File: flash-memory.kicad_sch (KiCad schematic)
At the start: 4 parts, among them U3 W25Q64JVZEIQ

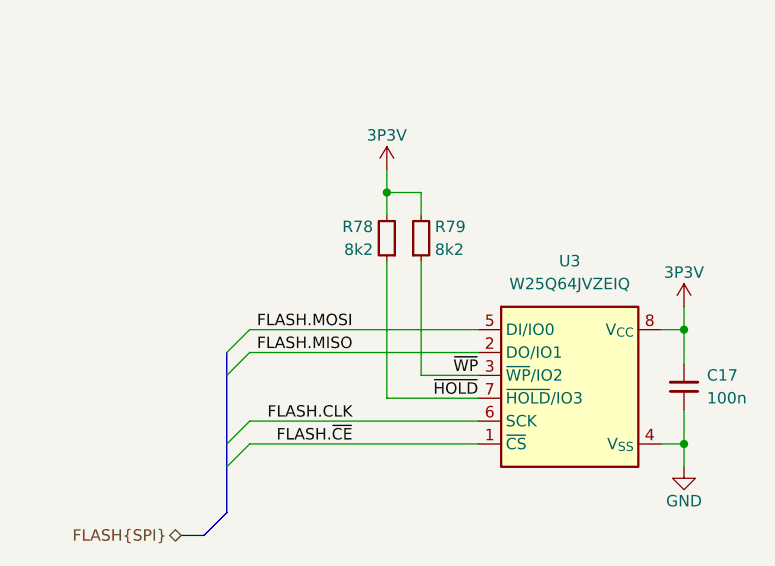
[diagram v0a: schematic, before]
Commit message: [#80813] Change RJ45 connectors, reannotate schematics
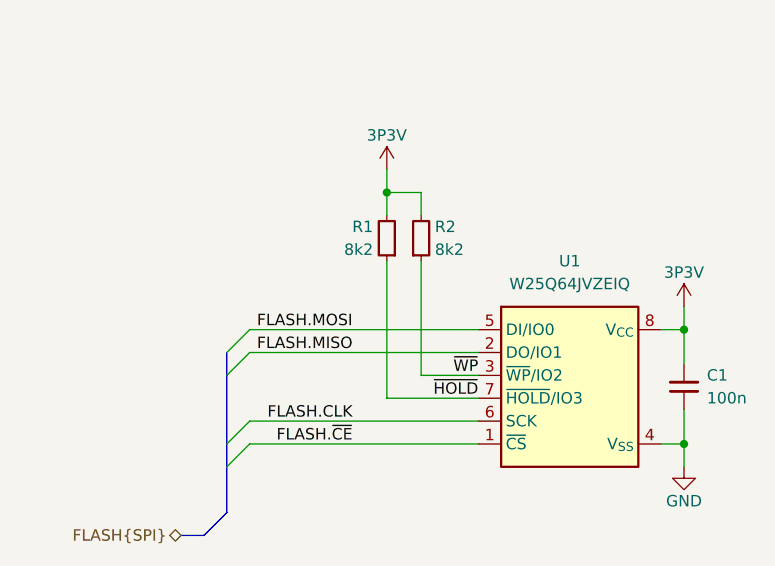
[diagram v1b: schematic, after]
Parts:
- renumbered C17 to C1, R78 to R1, R79 to R2, U3 to U1
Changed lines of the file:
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@@
 		(on_board yes)
 		(dnp no)
-		(property "Reference" "R78"
+		(property "Reference" "R1"
 			(at 191.516 132.08 90)
 			(effects
@@
 			(project ""
 				(path "/04bda987-e5eb-48b4-9e90-d8211dc11b39/cf61e8ef-a7e0-463f-9b69-1bf3871ad792"
-					(reference "R78")
+					(reference "R1")
 					(unit 1)
 				)
@@
 		(dnp no)
 		(fields_autoplaced yes)
-		(property "Reference" "U3"
+		(property "Reference" "U1"
 			(at 213.36 135.89 0)
 			(effects
@@
 			(project ""
 				(path "/04bda987-e5eb-48b4-9e90-d8211dc11b39/cf61e8ef-a7e0-463f-9b69-1bf3871ad792"
-					(reference "U3")
+					(reference "U1")
 					(unit 1)
 				)
@@
 		(on_board yes)
 		(dnp no)
-		(property "Reference" "#PWR076"
+		(property "Reference" "#PWR02"
 			(at 226.06 144.78 0)
 			(effects
@@
 			(project "10-gbe-expansion"
 				(path "/04bda987-e5eb-48b4-9e90-d8211dc11b39/cf61e8ef-a7e0-463f-9b69-1bf3871ad792"
-					(reference "#PWR076")
+					(reference "#PWR02")
 					(unit 1)
 				)
@@
 		(on_board yes)
 		(dnp no)
-		(property "Reference" "#PWR077"
+		(property "Reference" "#PWR01"
 			(at 193.04 129.54 0)
 			(effects
@@
 			(project "10-gbe-expansion"
 				(path "/04bda987-e5eb-48b4-9e90-d8211dc11b39/cf61e8ef-a7e0-463f-9b69-1bf3871ad792"
-					(reference "#PWR077")
+					(reference "#PWR01")
 					(unit 1)
 				)
@@
 		(dnp no)
 		(fields_autoplaced yes)
-		(property "Reference" "C17"
+		(property "Reference" "C1"
 			(at 228.6 148.5836 90)
 			(effects
@@
 			(project "10-gbe-expansion"
 				(path "/04bda987-e5eb-48b4-9e90-d8211dc11b39/cf61e8ef-a7e0-463f-9b69-1bf3871ad792"
-					(reference "C17")
+					(reference "C1")
 					(unit 1)
 				)
@@
 		(on_board yes)
 		(dnp no)
-		(property "Reference" "R79"
+		(property "Reference" "R2"
 			(at 198.374 132.08 90)
 			(effects
@@
 			(project "10-gbe-expansion"
 				(path "/04bda987-e5eb-48b4-9e90-d8211dc11b39/cf61e8ef-a7e0-463f-9b69-1bf3871ad792"
-					(reference "R79")
+					(reference "R2")
 					(unit 1)
 				)
@@
 		(on_board yes)
 		(dnp no)
-		(property "Reference" "#PWR075"
+		(property "Reference" "#PWR03"
 			(at 234.95 161.29 0)
 			(effects
@@
 			(project "10-gbe-expansion"
 				(path "/04bda987-e5eb-48b4-9e90-d8211dc11b39/cf61e8ef-a7e0-463f-9b69-1bf3871ad792"
-					(reference "#PWR075")
+					(reference "#PWR03")
 					(unit 1)
 				)

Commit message: [#80813] Change 3V3 and 1V88 power rails names
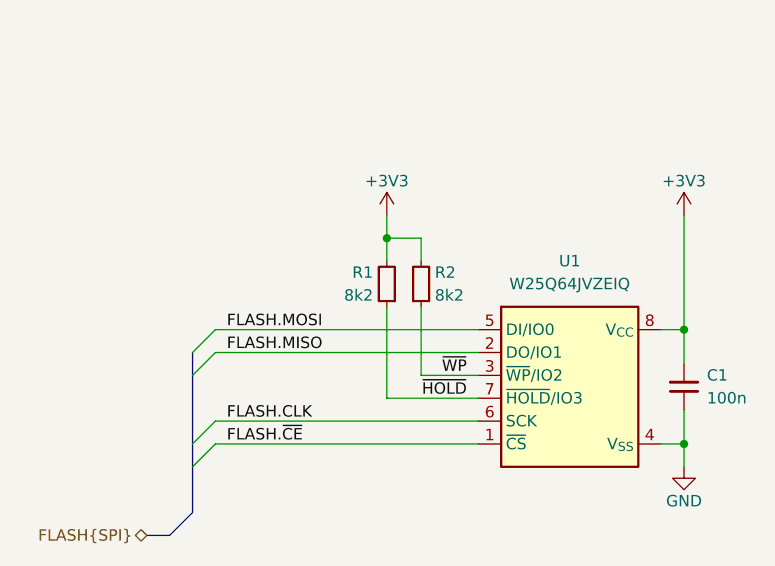
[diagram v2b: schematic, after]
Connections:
- net 3P3V renamed +3V3
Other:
- moved on the sheet: R1, R2

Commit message: [#80813] WIP: Adjust passives values, add missing load capacitors for the 50MHz resonator
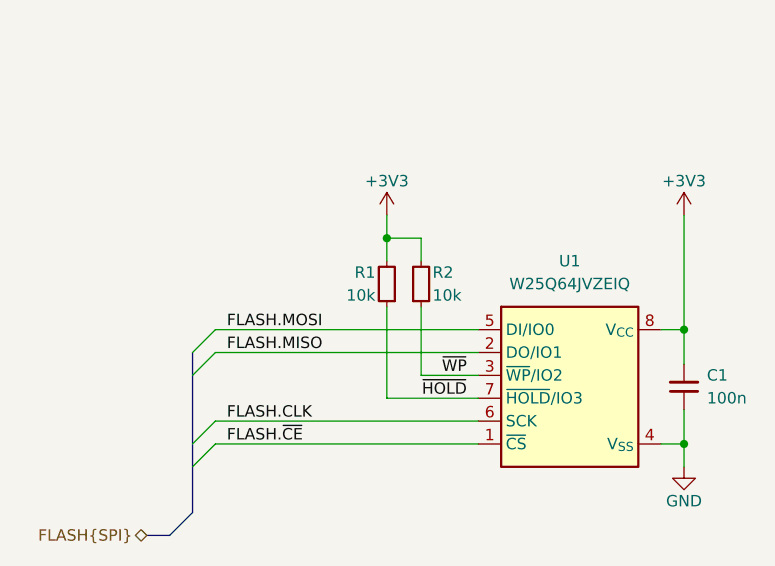
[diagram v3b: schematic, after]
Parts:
- removed R1, R2: R_8k2_0402, antmicro-footprints:R_0402_1005Metric, symbol antmicroResistors0402:R_8k2_0402
- added R1, R2: R_10k_0402, antmicro-footprints:R_0402_1005Metric, symbol antmicroResistors0402:R_10k_0402
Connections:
- net +3V3: now also R1.2, R2.2
- net ~{HOLD}: now also R1.1
- net ~{WP}: now also R2.1
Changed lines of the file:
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@@
-	)
-	(symbol
-		(lib_id "antmicroResistors0402:R_8k2_0402")
-		(at 193.04 140.97 270)
-		(mirror x)
-		(unit 1)
-		(exclude_from_sim no)
-		(in_bom yes)
-		(on_board yes)
-		(dnp no)
-		(property "Reference" "R1"
-			(at 191.516 137.16 90)
-			(effects
-				(font
-					(size 1.27 1.27)
-					(thickness 0.15)
-				)
-				(justify right)
-			)
-		)
-		(property "Value" "R_8k2_0402"
-			(at 180.34 120.65 0)
-			(effects
-				(font
-					(size 1.27 1.27)
-					(thickness 0.15)
-				)
-				(justify left bottom)
-				(hide yes)
-			)
-		)
-		(property "Footprint" "antmicro-footprints:R_0402_1005Metric"
-			(at 177.8 120.65 0)
-			(effects
-				(font
-					(size 1.27 1.27)
-					(thickness 0.15)
-				)
-				(justify left bottom)
-				(hide yes)
-			)
-		)
-		(property "Datasheet" "https://www.bourns.com/docs/product-datasheets/cr.pdf"
-			(at 175.26 120.65 0)
-			(effects
-				(font
-					(size 1.27 1.27)
-					(thickness 0.15)
-				)
-				(justify left bottom)
-				(hide yes)
-			)
-		)
-		(property "Description" "SMD Chip Resistor"
-			(at 193.04 140.97 0)
-			(effects
-				(font
-					(size 1.27 1.27)
-				)
-				(hide yes)
-			)
-		)
-		(property "MPN" "CR0402-FX-8201GLF"
-			(at 172.72 120.65 0)
-			(effects
-				(font
-					(size 1.27 1.27)
-					(thickness 0.15)
-				)
-				(justify left bottom)
-				(hide yes)
-			)
-		)
-		(property "Manufacturer" "Bourns"
-			(at 170.18 120.65 0)
-			(effects
-				(font
-					(size 1.27 1.27)
-					(thickness 0.15)
-				)
-				(justify left bottom)
-				(hide yes)
-			)
-		)
-		(property "License" "Apache-2.0"
-			(at 167.64 120.65 0)
-			(effects
-				(font
-					(size 1.27 1.27)
-					(thickness 0.15)
-				)
-				(justify left bottom)
-				(hide yes)
-			)
-		)
-		(property "Author" "Antmicro"
-			(at 165.1 120.65 0)
-			(effects
-				(font
-					(size 1.27 1.27)
-					(thickness 0.15)
-				)
-				(justify left bottom)
-				(hide yes)
-			)
-		)
-		(property "Val" "8k2"
-			(at 191.516 139.7 90)
-			(effects
-				(font
-					(size 1.27 1.27)
-					(thickness 0.15)
-				)
-				(justify right)
-			)
-		)
-		(property "Tolerance" "1%"
-			(at 182.88 120.65 0)
-			(effects
-				(font
-					(size 1.27 1.27)
-				)
-				(justify left bottom)
-				(hide yes)
-			)
-		)
-		(pin "2"
-		)
-		(pin "1"
-		)
-		(instances
-			(project ""
-				(path "/04bda987-e5eb-48b4-9e90-d8211dc11b39/cf61e8ef-a7e0-463f-9b69-1bf3871ad792"
-					(reference "R1")
-					(unit 1)
-				)
-			)
-		)
 	)
 	(symbol
@@
 	)
 	(symbol
+		(lib_id "antmicroResistors0402:R_10k_0402")
+		(at 193.04 140.97 270)
+		(mirror x)
+		(unit 1)
+		(exclude_from_sim no)
+		(in_bom yes)
+		(on_board yes)
+		(dnp no)
+		(property "Reference" "R1"
+			(at 191.77 137.16 90)
+			(effects
+				(font
+					(size 1.27 1.27)
+					(thickness 0.15)
+				)
+				(justify right)
+			)
+		)
+		(property "Value" "R_10k_0402"
+			(at 180.34 120.65 0)
+			(effects
+				(font
+					(size 1.27 1.27)
+					(thickness 0.15)
+				)
+				(justify left bottom)
+				(hide yes)
+			)
+		)
+		(property "Footprint" "antmicro-footprints:R_0402_1005Metric"
+			(at 177.8 120.65 0)
+			(effects
+				(font
+					(size 1.27 1.27)
+					(thickness 0.15)
+				)
+				(justify left bottom)
+				(hide yes)
+			)
+		)
+		(property "Datasheet" "https://www.bourns.com/docs/product-datasheets/cr.pdf"
+			(at 175.26 120.65 0)
+			(effects
+				(font
+					(size 1.27 1.27)
+					(thickness 0.15)
+				)
+				(justify left bottom)
+				(hide yes)
+			)
+		)
+		(property "Description" "SMD Chip Resistor, 10 kohm, ± 1%, 62.5 mW, 0402 [1005 Metric], Thick Film, General Purpose"
+			(at 193.04 140.97 0)
+			(effects
+				(font
+					(size 1.27 1.27)
+				)
+				(hide yes)
+			)
+		)
+		(property "MPN" "CR0402-FX-1002GLF"
+			(at 172.72 120.65 0)
+			(effects
+				(font
+					(size 1.27 1.27)
+					(thickness 0.15)
+				)
+				(justify left bottom)
+				(hide yes)
+			)
+		)
+		(property "Manufacturer" "Bourns"
+			(at 170.18 120.65 0)
+			(effects
+				(font
+					(size 1.27 1.27)
+					(thickness 0.15)
+				)
+				(justify left bottom)
+				(hide yes)
+			)
+		)
+		(property "License" "Apache-2.0"
+			(at 167.64 120.65 0)
+			(effects
+				(font
+					(size 1.27 1.27)
+					(thickness 0.15)
+				)
+				(justify left bottom)
+				(hide yes)
+			)
+		)
+		(property "Author" "Antmicro"
+			(at 165.1 120.65 0)
+			(effects
+				(font
+					(size 1.27 1.27)
+					(thickness 0.15)
+				)
+				(justify left bottom)
+				(hide yes)
+			)
+		)
+		(property "Val" "10k"
+			(at 191.77 139.7 90)
+			(effects
+				(font
+					(size 1.27 1.27)
+					(thickness 0.15)
+				)
+				(justify right)
+			)
+		)
+		(property "Tolerance" "1%"
+			(at 182.88 120.65 0)
+			(effects
+				(font
+					(size 1.27 1.27)
+				)
+				(justify left bottom)
+				(hide yes)
+			)
+		)
+		(pin "1"
+		)
+		(pin "2"
+		)
+		(instances
+			(project "10-gbe-expansion"
+				(path "/04bda987-e5eb-48b4-9e90-d8211dc11b39/cf61e8ef-a7e0-463f-9b69-1bf3871ad792"
+					(reference "R1")
+					(unit 1)
+				)
+			)
+		)
+	)
+	(symbol
 		(lib_id "antmicropower:+3V3")
 		(at 226.06 130.81 0)
@@
 	)
 	(symbol
-		(lib_id "antmicroResistors0402:R_8k2_0402")
+		(lib_id "antmicroResistors0402:R_10k_0402")
 		(at 196.85 140.97 90)
 		(unit 1)
@@
 		(dnp no)
 		(property "Reference" "R2"
-			(at 198.374 137.16 90)
+			(at 198.12 137.16 90)
 			(effects
 				(font
@@
 			)
 		)
-		(property "Value" "R_8k2_0402"
+		(property "Value" "R_10k_0402"
 			(at 209.55 120.65 0)
 			(effects
@@
 			)
 		)
-		(property "Description" "SMD Chip Resistor"
+		(property "Description" "SMD Chip Resistor, 10 kohm, ± 1%, 62.5 mW, 0402 [1005 Metric], Thick Film, General Purpose"
 			(at 196.85 140.97 0)
 			(effects
@@
 			)
 		)
-		(property "MPN" "CR0402-FX-8201GLF"
+		(property "MPN" "CR0402-FX-1002GLF"
 			(at 217.17 120.65 0)
 			(effects
@@
 			)
 		)
-		(property "Val" "8k2"
-			(at 198.374 139.7 90)
+		(property "Val" "10k"
+			(at 198.12 139.7 90)
 			(effects
 				(font
@@
 			)
 		)
+		(pin "1"
+		)
 		(pin "2"
 		)
-		(pin "1"
-		)
 		(instances
-			(project "10-gbe-expansion"
+			(project ""
 				(path "/04bda987-e5eb-48b4-9e90-d8211dc11b39/cf61e8ef-a7e0-463f-9b69-1bf3871ad792"
 					(reference "R2")

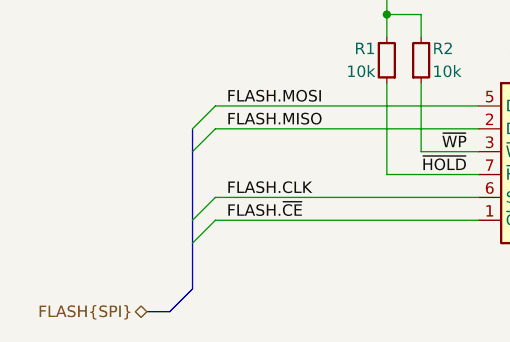
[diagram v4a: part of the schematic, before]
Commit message: [#80813] Change inductors, minor PCB changes
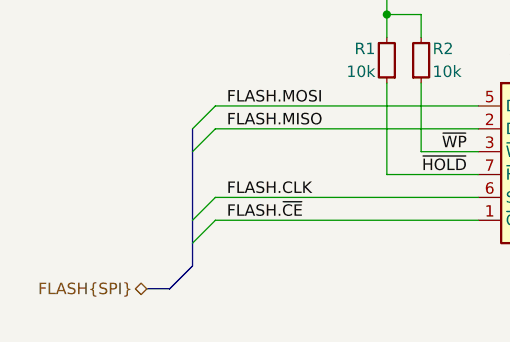
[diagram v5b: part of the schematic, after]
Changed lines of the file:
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@@
 	(bus
 		(pts
-			(xy 168.91 166.37) (xy 171.45 163.83)
+			(xy 168.91 163.83) (xy 171.45 161.29)
 		)
 		(stroke
@@
 	(bus
 		(pts
-			(xy 168.91 166.37) (xy 166.37 166.37)
+			(xy 168.91 163.83) (xy 166.37 163.83)
 		)
 		(stroke
@@
 	(bus
 		(pts
-			(xy 171.45 158.75) (xy 171.45 163.83)
+			(xy 171.45 158.75) (xy 171.45 161.29)
 		)
 		(stroke
@@
 	(hierarchical_label "FLASH{SPI}"
 		(shape bidirectional)
-		(at 166.37 166.37 180)
-		(effects
-			(font
+		(at 166.37 163.83 180)
+		(effects
+			(font

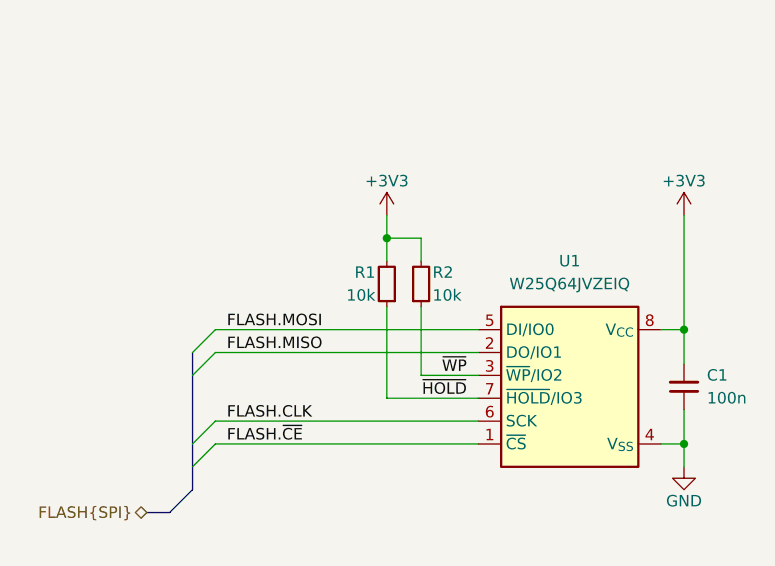
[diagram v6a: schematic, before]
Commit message: [#85196] Clear ERC, minor schematic fixes
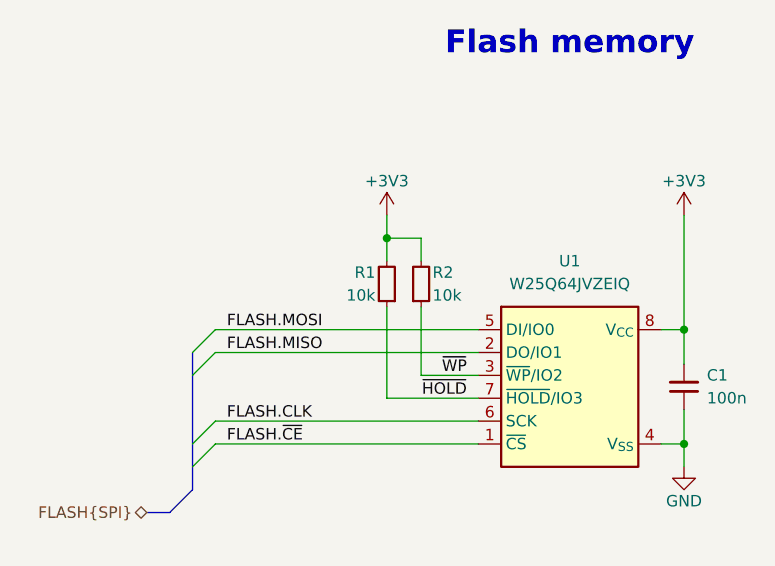
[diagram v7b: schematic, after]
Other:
- note added: "Flash memory"
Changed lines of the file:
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@@
 		(comment 1 "www.antmicro.com")
+	)
+	(text "Flash memory"
+		(exclude_from_sim no)
+		(at 213.36 111.76 0)
+		(effects
+			(font
+				(size 2.54 2.54)
+				(thickness 0.508)
+				(bold yes)
+			)
+		)
 	)
 	(junction

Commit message: [#85196] Re-annotate schematic
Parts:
- renumbered C1 to C47, R1 to R34, R2 to R35, U1 to U6
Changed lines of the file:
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@@
 		(on_board yes)
 		(dnp no)
-		(property "Reference" "#PWR07"
+		(property "Reference" "#PWR063"
 			(at 208.28 130.81 0)
 			(effects
@@
 			(project "10-gbe-expansion"
 				(path "/04bda987-e5eb-48b4-9e90-d8211dc11b39/cf61e8ef-a7e0-463f-9b69-1bf3871ad792"
-					(reference "#PWR07")
+					(reference "#PWR063")
 					(unit 1)
 				)
@@
 		(dnp no)
 		(fields_autoplaced yes)
-		(property "Reference" "U1"
+		(property "Reference" "U6"
 			(at 213.36 135.89 0)
 			(effects
@@
 			(project ""
 				(path "/04bda987-e5eb-48b4-9e90-d8211dc11b39/cf61e8ef-a7e0-463f-9b69-1bf3871ad792"
-					(reference "U1")
+					(reference "U6")
 					(unit 1)
 				)
@@
 		(on_board yes)
 		(dnp no)
-		(property "Reference" "R1"
+		(property "Reference" "R34"
 			(at 191.77 137.16 90)
 			(effects
@@
 			(project "10-gbe-expansion"
 				(path "/04bda987-e5eb-48b4-9e90-d8211dc11b39/cf61e8ef-a7e0-463f-9b69-1bf3871ad792"
-					(reference "R1")
+					(reference "R34")
 					(unit 1)
 				)
@@
 		(on_board yes)
 		(dnp no)
-		(property "Reference" "#PWR08"
+		(property "Reference" "#PWR064"
 			(at 241.3 130.81 0)
 			(effects
@@
 			(project "10-gbe-expansion"
 				(path "/04bda987-e5eb-48b4-9e90-d8211dc11b39/cf61e8ef-a7e0-463f-9b69-1bf3871ad792"
-					(reference "#PWR08")
+					(reference "#PWR064")
 					(unit 1)
 				)
@@
 		(dnp no)
 		(fields_autoplaced yes)
-		(property "Reference" "C1"
+		(property "Reference" "C47"
 			(at 228.6 148.5836 90)
 			(effects
@@
 			(project "10-gbe-expansion"
 				(path "/04bda987-e5eb-48b4-9e90-d8211dc11b39/cf61e8ef-a7e0-463f-9b69-1bf3871ad792"
-					(reference "C1")
+					(reference "C47")
 					(unit 1)
 				)
@@
 		(on_board yes)
 		(dnp no)
-		(property "Reference" "R2"
+		(property "Reference" "R35"
 			(at 198.12 137.16 90)
 			(effects
@@
 			(project ""
 				(path "/04bda987-e5eb-48b4-9e90-d8211dc11b39/cf61e8ef-a7e0-463f-9b69-1bf3871ad792"
-					(reference "R2")
+					(reference "R35")
 					(unit 1)
 				)
@@
 		(on_board yes)
 		(dnp no)
-		(property "Reference" "#PWR09"
+		(property "Reference" "#PWR065"
 			(at 234.95 161.29 0)
 			(effects
@@
 			(project "10-gbe-expansion"
 				(path "/04bda987-e5eb-48b4-9e90-d8211dc11b39/cf61e8ef-a7e0-463f-9b69-1bf3871ad792"
-					(reference "#PWR09")
+					(reference "#PWR065")
 					(unit 1)
 				)
